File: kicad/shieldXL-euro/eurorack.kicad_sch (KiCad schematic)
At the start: 49 parts, among them J101 Eurorack power, J102 IN L, J103 IN R, J104 OUT L, J105 OUT R, J106 MIDI IN, J107 MIDI OUT, J108 DX07S024WJ1R350, J109 USB 1, J110 USB 2, J111 USB 3, J112 Pi USB, inner stack, J113 Pi USB, outer stack, J115 CORONE I/1, J116 CORONE I/2, J117 CORONE O/1, J118 CORONE O/2, J119 CORONE O/3, J120 CORONE O/4, J121 Corone, J122 ii, U101 TL074

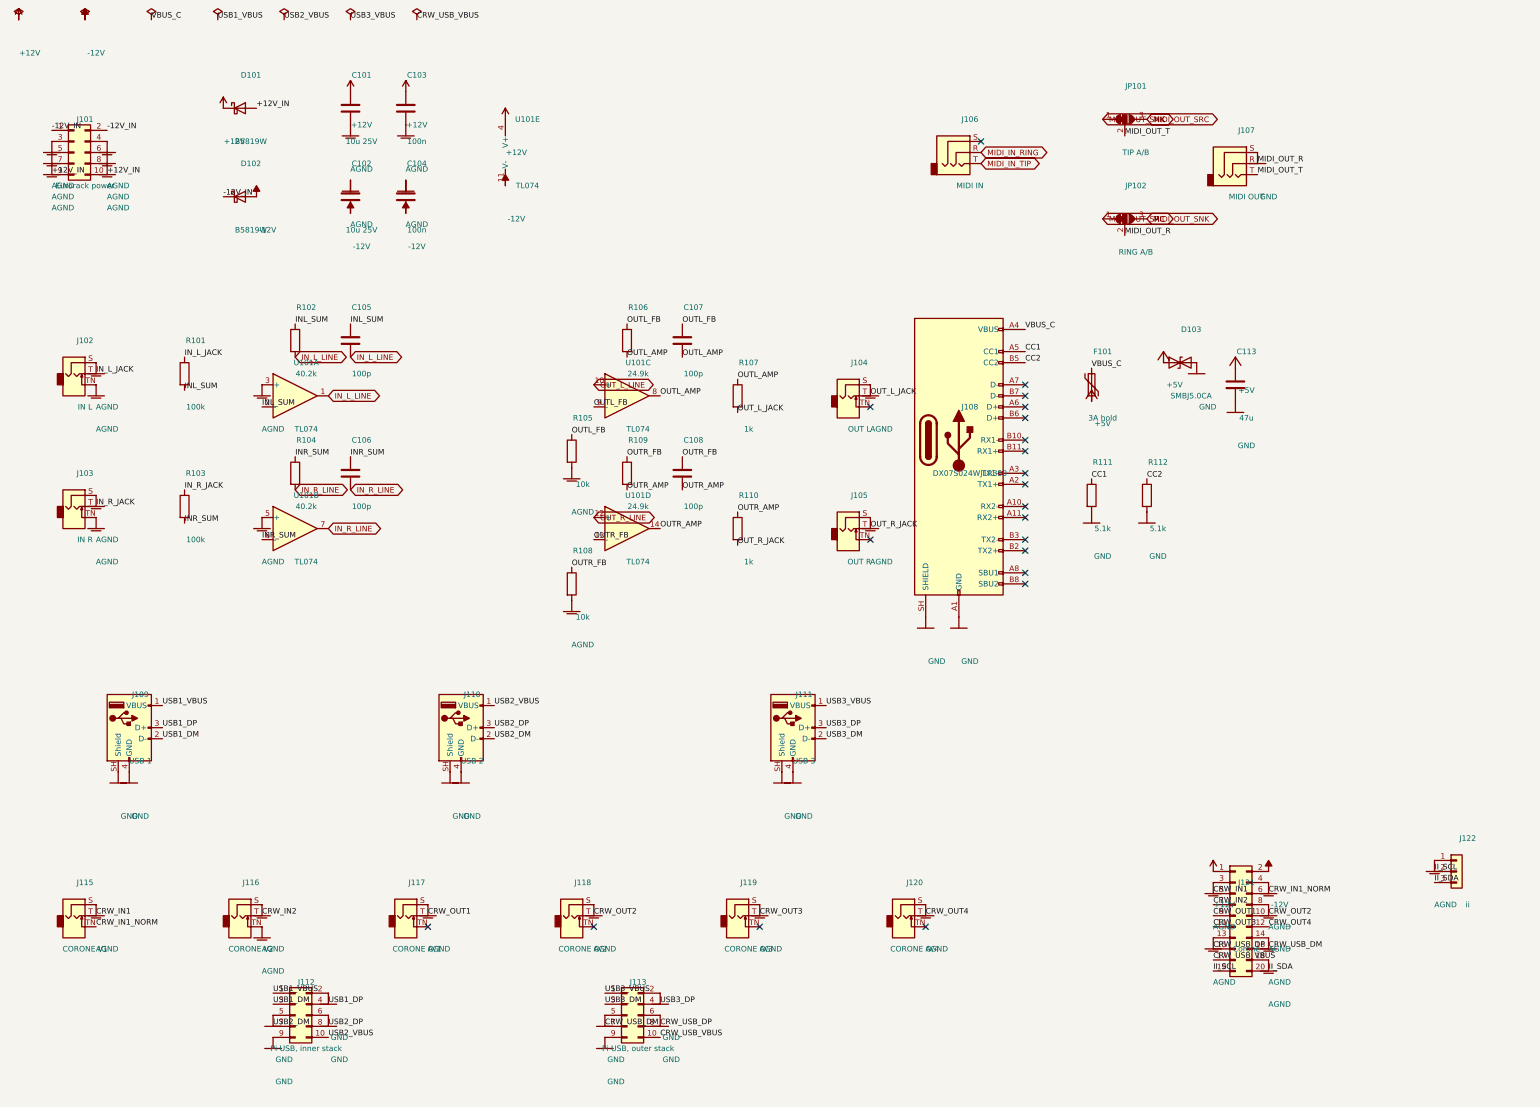
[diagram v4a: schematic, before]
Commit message: Circuit review: USB ESD and bulk, MIDI out buffer, panel MIDI LEDs, non-inverting inputs, display decoupling, AGND-GND jumper
- U102-U104 USBLC6-2SC6 on each panel USB-A's D+/D-, with 47u + 100n on
  its VBUS (C114-C119): the ports are on the panel, the Pi 10 cm away.
- U105 74LVC1G125 between the Pi's TXD and the MIDI out resistor and TX LED
  (MIDI_TX -> MIDI_TX_BUF): a TRS plug going in shorts tip/ring to sleeve,
  and the buffer takes that, not the Pi. R17 47 -> 100 ohm keeps that
  short under the buffer's 50 mA and the loop at about 5 mA.
- D1 / D2 come out to the panel: red 3 mm LEDs (MMM:LED_3mm_PadsAC, pads
  named A/C for shieldXL's symbol) between the MIDI jacks, 470 ohm each.
- Inputs: 69.8k / 30.1k divider into a follower instead of the inverting
  stage, so audio keeps its polarity; 13.4 Vpp reaches codec full scale.
- C121 / C122 10u + 100n on +3V3 at the display's FPC connector.
- JP103, open, across the AGND-GND ferrite L3.

Co-Authored-By: Claude Opus 5.5 <noreply@anthropic.com>
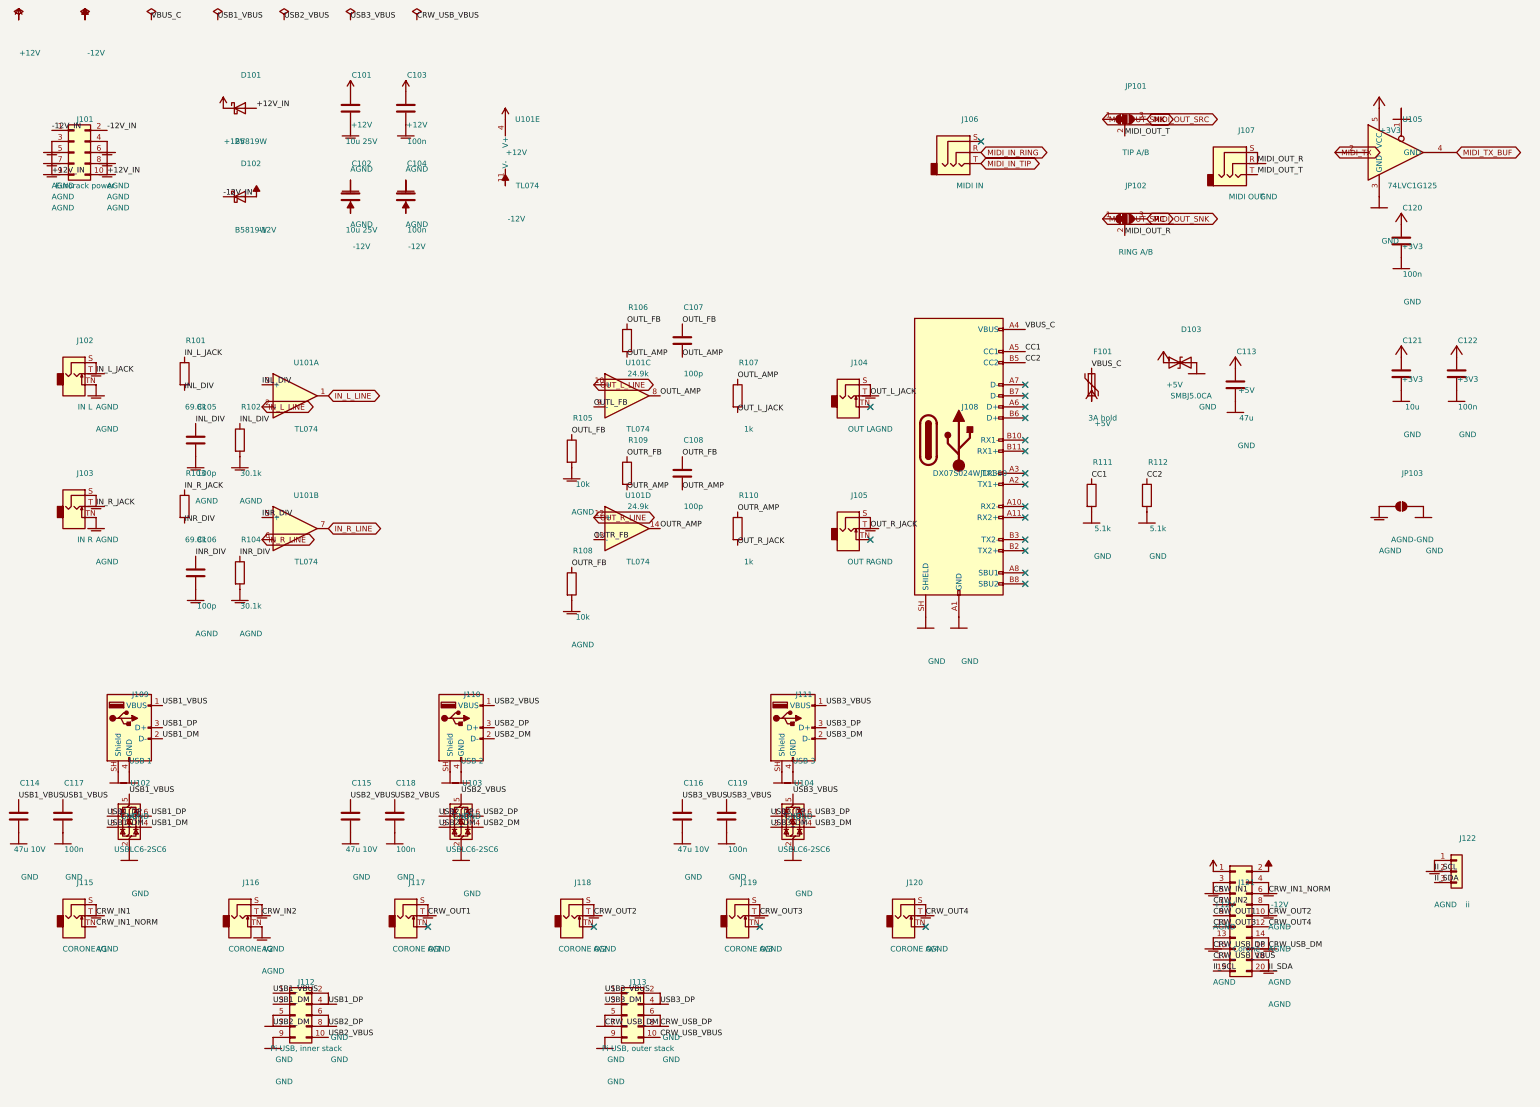
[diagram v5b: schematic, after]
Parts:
- added C114, C115, C116: 47u 10V, Capacitor_SMD:C_1206_3216Metric, symbol Device:C
- added C117, C118, C119, C120, C122: 100n, Capacitor_SMD:C_0805_2012Metric, symbol Device:C
- added C121: 10u, Capacitor_SMD:C_0805_2012Metric, symbol Device:C
- added JP103: AGND-GND, Jumper:SolderJumper-2_P1.3mm_Open_Pad1.0x1.5mm, symbol Jumper:SolderJumper_2_Open
- added U102, U103, U104: USBLC6-2SC6, Package_TO_SOT_SMD:SOT-23-6, symbol Power_Protection:USBLC6-2P6
- added U105: 74LVC1G125, Package_TO_SOT_SMD:SOT-23-5, symbol 74xGxx:74LVC1G125
- R101, R103: value 100k -> 69.8k
- R102, R104: value 40.2k -> 30.1k
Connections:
- net AGND: now also C105.2, C106.2, R102.2, R104.2, JP103.1 (A); no longer U101.3 (+), U101.5 (+)
- net GND: now also C114.2, C115.2, C116.2, C117.2, C118.2, C119.2, C120.2, C121.2, C122.2, JP103.2 (B), U102.2 (GND), U103.2 (GND), U104.2 (GND), U105.1, U105.3 (GND)
- net IN_L_LINE: now also U101.2 (-); no longer C105.2, R102.2
- net IN_R_LINE: now also U101.6 (-); no longer C106.2, R104.2
- net USB1_DM: now also U102.3 (I/O2), U102.4 (I/O2)
- net USB1_DP: now also U102.1 (I/O1), U102.6 (I/O1)
- net USB1_VBUS: now also C114.1, C117.1, U102.5 (VBUS)
- net USB2_DM: now also U103.3 (I/O2), U103.4 (I/O2)
- net USB2_DP: now also U103.1 (I/O1), U103.6 (I/O1)
- net USB2_VBUS: now also C115.1, C118.1, U103.5 (VBUS)
- net USB3_DM: now also U104.3 (I/O2), U104.4 (I/O2)
- net USB3_DP: now also U104.1 (I/O1), U104.6 (I/O1)
- net USB3_VBUS: now also C116.1, C119.1, U104.5 (VBUS)
- net INL_SUM renamed INL_DIV
- net INL_DIV: now also U101.3 (+); no longer U101.2 (-)
- net INR_SUM renamed INR_DIV
- net INR_DIV: now also U101.5 (+); no longer U101.6 (-)
- new net +3V3: C120.1, C121.1, C122.1, U105.5 (VCC)
- new net MIDI_TX: U105.2
- new net MIDI_TX_BUF: U105.4
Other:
- moved on the sheet: R102

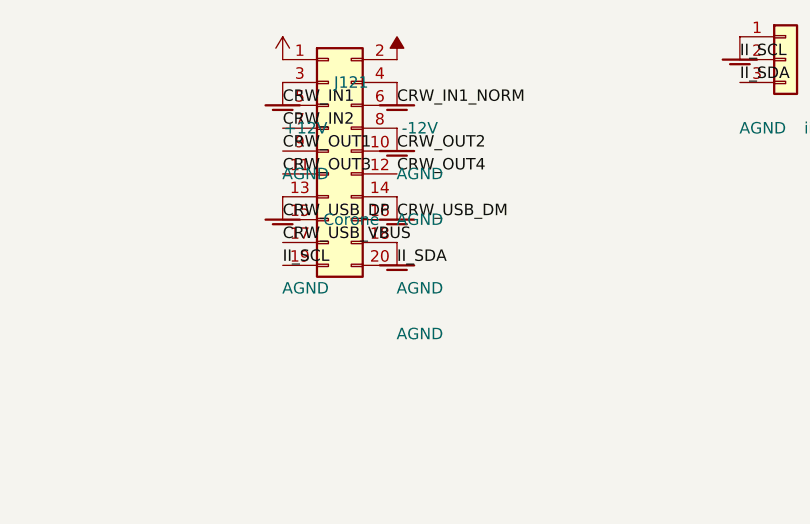
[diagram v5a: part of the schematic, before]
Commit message: Corone header: swap pins 17 and 18 (GND on 17, USB VBUS sense on 18)
Both sides of the 2x10: J121 on the main board, J1 on Corone, and the
pinout in corone/README.md. For routing; electrically the same.

Co-Authored-By: Claude Opus 5.5 <noreply@anthropic.com>
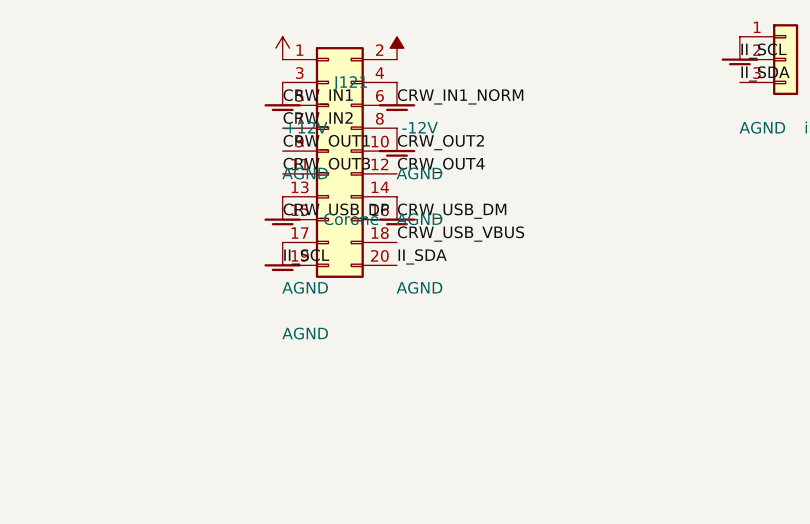
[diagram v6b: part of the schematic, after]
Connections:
- net AGND: now also J121.17 (Pin_17); no longer J121.18 (Pin_18)
- net CRW_USB_VBUS: now also J121.18 (Pin_18); no longer J121.17 (Pin_17)
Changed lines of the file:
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@@
-		)
-	)
-	(label "CRW_USB_VBUS"
-		(at 299.72 236.22 0)
-		(effects
-			(font
-				(size 1.27 1.27)
-			)
-			(justify left bottom)
 		)
 	)
 	(symbol
 		(lib_id "norns-shield-210330-eagle-import:AGND")
-		(at 312.42 238.76 0)
+		(at 299.72 238.76 0)
 		(unit 1)
 		(exclude_from_sim no)
@@
 		(dnp no)
 		(property "Reference" "#PWR155"
-			(at 314.96 231.14 0)
+			(at 302.26 231.14 0)
 			(hide yes)
 			(effects
@@
 		)
 		(property "Value" "AGND"
-			(at 314.96 246.38 0)
+			(at 302.26 246.38 0)
 			(effects
 				(font
@@
 		)
 		(property "Footprint" ""
-			(at 312.42 238.76 0)
+			(at 299.72 238.76 0)
 			(hide yes)
 			(effects
@@
 		)
 		(property "Datasheet" ""
-			(at 312.42 238.76 0)
+			(at 299.72 238.76 0)
 			(hide yes)
 			(effects
@@
 		)
 	)
+	(label "CRW_USB_VBUS"
+		(at 312.42 236.22 0)
+		(effects
+			(font
+				(size 1.27 1.27)
+			)
+			(justify left bottom)
+		)
+	)

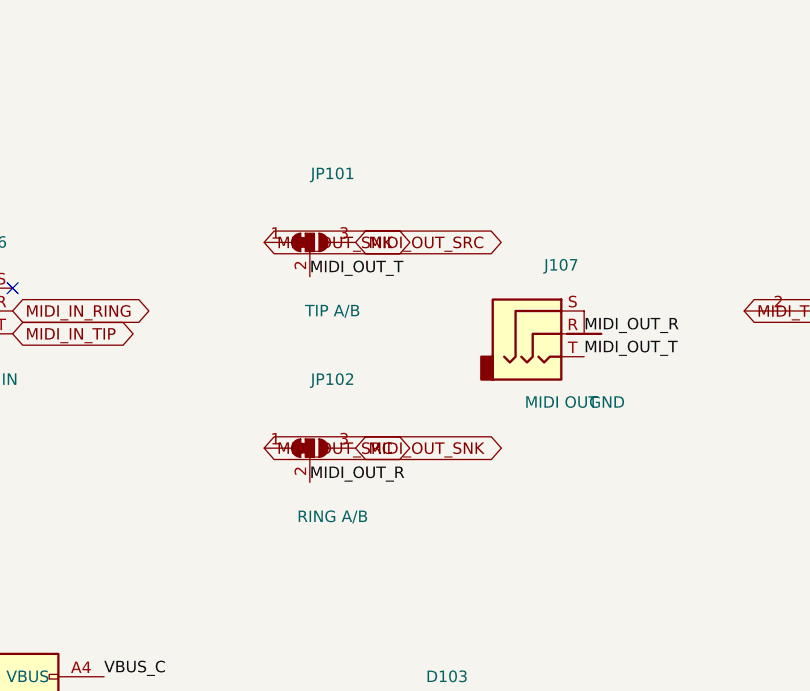
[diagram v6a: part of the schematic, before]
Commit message: MIDI out A/B: 2 x 3 header and shunts (J123) in place of the solder jumpers
Odd pins the tip, even the ring, the middle row the jack: both shunts on
the top row is Type A, on the bottom row Type B. J123 keeps JP101's
symbol id, so the board links without Update PCB; its tracks are left to
route. Also takes in the board edits saved since the last commit.

Co-Authored-By: Claude Opus 5.5 <noreply@anthropic.com>
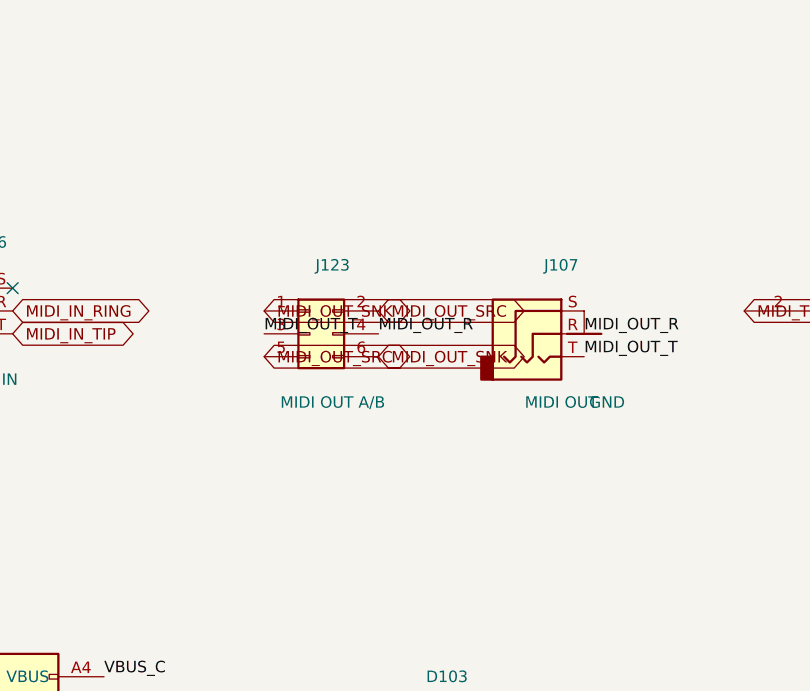
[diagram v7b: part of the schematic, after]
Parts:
- removed JP102: RING A/B, Jumper:SolderJumper-3_P1.3mm_Bridged12_Pad1.0x1.5mm, symbol Jumper:SolderJumper_3_Bridged12
- J123: renamed from JP101; value TIP A/B -> MIDI OUT A/B; footprint Jumper:SolderJumper-3_P1.3mm_Bridged12_Pad1.0x1.5mm -> Connector_PinHeader_2.54mm:PinHeader_2x03_P2.54mm_Vertical; symbol Jumper:SolderJumper_3_Bridged12 -> Connector_Generic:Conn_02x03_Odd_Even; now in the parts list
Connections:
- net MIDI_OUT_R: now also J123.4 (Pin_4)
- net MIDI_OUT_SNK: now also J123.6 (Pin_6)
- net MIDI_OUT_SRC: now also J123.2 (Pin_2), J123.5 (Pin_5); no longer J123.3 (B)
- net MIDI_OUT_T: now also J123.3 (Pin_3); no longer J123.2 (C)
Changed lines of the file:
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@@
 	)
 	(symbol
-		(lib_id "Jumper:SolderJumper_3_Bridged12")
-		(at 279.4 43.18 0)
+		(lib_id "Connector_Generic:Conn_02x03_Odd_Even")
+		(at 279.4 53.34 0)
 		(unit 1)
 		(exclude_from_sim no)
-		(in_bom no)
+		(in_bom yes)
 		(on_board yes)
 		(dnp no)
-		(property "Reference" "JP101"
-			(at 281.94 35.56 0)
+		(property "Reference" "J123"
+			(at 281.94 45.72 0)
 			(effects
 				(font
@@
 			)
 		)
-		(property "Value" "TIP A/B"
-			(at 281.94 50.8 0)
+		(property "Value" "MIDI OUT A/B"
+			(at 281.94 60.96 0)
 			(effects
 				(font
@@
 			)
 		)
-		(property "Footprint" "Jumper:SolderJumper-3_P1.3mm_Bridged12_Pad1.0x1.5mm"
-			(at 279.4 43.18 0)
+		(property "Footprint" "Connector_PinHeader_2.54mm:PinHeader_2x03_P2.54mm_Vertical"
+			(at 279.4 53.34 0)
 			(hide yes)
 			(effects
@@
 		)
 		(property "Datasheet" ""
-			(at 279.4 43.18 0)
+			(at 279.4 53.34 0)
 			(hide yes)
 			(effects
@@
 		(pin "3"
 		)
+		(pin "4"
+		)
+		(pin "5"
+		)
+		(pin "6"
+		)
 		(instances
 			(project "shieldXL-euro"
 				(path "/b86e8947-58dc-49c6-bb5d-ce6d33c2e465/291b9154-df7e-5c77-b48b-0f7a699ae26f"
-					(reference "JP101")
+					(reference "J123")
 					(unit 1)
 				)
@@
 	(global_label "MIDI_OUT_SNK"
 		(shape bidirectional)
-		(at 274.32 43.18 0)
+		(at 274.32 50.8 0)
 		(effects
 			(font
@@
 		)
 		(property "Intersheetrefs" "${INTERSHEET_REFS}"
-			(at 274.32 43.18 0)
+			(at 274.32 50.8 0)
+			(effects
+				(font
+					(size 1.27 1.27)
+				)
+				(hide yes)
+			)
+		)
+	)
+	(global_label "MIDI_OUT_SRC"
+		(shape bidirectional)
+		(at 287.02 50.8 0)
+		(effects
+			(font
+				(size 1.27 1.27)
+			)
+			(justify left bottom)
+		)
+		(property "Intersheetrefs" "${INTERSHEET_REFS}"
+			(at 287.02 50.8 0)
 			(effects
 				(font
@@
 	)
 	(label "MIDI_OUT_T"
-		(at 279.4 46.99 0)
+		(at 274.32 53.34 0)
+		(effects
+			(font
+				(size 1.27 1.27)
+			)
+			(justify left bottom)
+		)
+	)
+	(label "MIDI_OUT_R"
+		(at 287.02 53.34 0)
 		(effects
 			(font
@@
 	(global_label "MIDI_OUT_SRC"
 		(shape bidirectional)
-		(at 284.48 43.18 0)
+		(at 274.32 55.88 0)
 		(effects
 			(font
@@
 		)
 		(property "Intersheetrefs" "${INTERSHEET_REFS}"
-			(at 284.48 43.18 0)
+			(at 274.32 55.88 0)
 			(effects
 				(font
@@
 		)
 	)
-	(symbol
-		(lib_id "Jumper:SolderJumper_3_Bridged12")
-		(at 279.4 66.04 0)
-		(unit 1)
-		(exclude_from_sim no)
-		(in_bom no)
-		(on_board yes)
-		(dnp no)
-		(property "Reference" "JP102"
-			(at 281.94 58.42 0)
-			(effects
-				(font
-					(size 1.27 1.27)
-				)
-			)
-		)
-		(property "Value" "RING A/B"
-			(at 281.94 73.66 0)
-			(effects
-				(font
-					(size 1.27 1.27)
-				)
-			)
-		)
-		(property "Footprint" "Jumper:SolderJumper-3_P1.3mm_Bridged12_Pad1.0x1.5mm"
-			(at 279.4 66.04 0)
-			(hide yes)
-			(effects
-				(font
-					(size 1.27 1.27)
-				)
-			)
-		)
-		(property "Datasheet" ""
-			(at 279.4 66.04 0)
-			(hide yes)
-			(effects
-				(font
-					(size 1.27 1.27)
-				)
-			)
-		)
-		(pin "1"
-		)
-		(pin "2"
-		)
-		(pin "3"
-		)
-		(instances
-			(project "shieldXL-euro"
-				(path "/b86e8947-58dc-49c6-bb5d-ce6d33c2e465/291b9154-df7e-5c77-b48b-0f7a699ae26f"
-					(reference "JP102")
-					(unit 1)
-				)
-			)
-		)
-	)
-	(global_label "MIDI_OUT_SRC"
+	(global_label "MIDI_OUT_SNK"
 		(shape bidirectional)
-		(at 274.32 66.04 0)
+		(at 287.02 55.88 0)
 		(effects
 			(font
@@
 		)
 		(property "Intersheetrefs" "${INTERSHEET_REFS}"
-			(at 274.32 66.04 0)
+			(at 287.02 55.88 0)
 			(effects
 				(font
-					(size 1.27 1.27)
-				)
-				(hide yes)
-			)
-		)
-	)
-	(label "MIDI_OUT_R"
-		(at 279.4 69.85 0)
-		(effects
-			(font
-				(size 1.27 1.27)
-			)
-			(justify left bottom)
-		)
-	)
-	(global_label "MIDI_OUT_SNK"
-		(shape bidirectional)
-		(at 284.48 66.04 0)
-		(effects
-			(font
-				(size 1.27 1.27)
-			)
-			(justify left bottom)
-		)
-		(property "Intersheetrefs" "${INTERSHEET_REFS}"
-			(at 284.48 66.04 0)
-			(effects
-				(font
